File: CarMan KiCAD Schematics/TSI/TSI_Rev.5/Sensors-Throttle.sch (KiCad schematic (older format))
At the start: 56 parts, among them IC1 TS431ILT, J13 Conn_01x01, J24 Conn_01x01, J25 Conn_01x01, J26 J26, J27 J27, J28 Conn_01x01, U21 MCP6004, U25 NCD9830DBR2G, U26 MCP6004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

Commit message: - Updating TSI
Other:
- note added: "THROTTLE VOLTAGE ISOLATOR"
- note removed: "V/I\n& THROTTLE VOLTAGE ISOLATOR"
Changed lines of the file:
@@
 Text Notes 6950 6600 0    98   ~ 0
 Binary Address:\n1001010
-Text Notes 12100 10450 0    157  ~ 0
-V/I\n& THROTTLE VOLTAGE ISOLATOR
+Text Notes 12200 10350 0    157  ~ 0
+THROTTLE VOLTAGE ISOLATOR
 Text Label 6400 9600 2    50   ~ 0
 A2_HV

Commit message: Renumbered headers & changed some footprints
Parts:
- J24: renamed from J13; value Conn_01x01 -> MC+ Short Pin 1; footprint Connector_PinHeader_1.00mm:PinHeader_1x01_P1.00mm_Vertical -> Connector_PinSocket_2.54mm:PinSocket_1x01_P2.54mm_Vertical
- J25: renamed from J28; value Conn_01x01 -> MC+ Short Pin 2; footprint Connector_PinHeader_1.00mm:PinHeader_1x01_P1.00mm_Vertical -> Connector_PinSocket_2.54mm:PinSocket_1x01_P2.54mm_Vertical
- J26: value J26 -> HV+ Short Pin 1; footprint Connector_PinHeader_1.00mm:PinHeader_1x01_P1.00mm_Vertical -> Connector_PinSocket_2.54mm:PinSocket_1x01_P2.54mm_Vertical
- J27: renamed from J24; value Conn_01x01 -> HV+ Short Pin 2; footprint Connector_PinHeader_1.00mm:PinHeader_1x01_P1.00mm_Vertical -> Connector_PinSocket_2.54mm:PinSocket_1x01_P2.54mm_Vertical
- J28: renamed from J27; value J27 -> HV- Short Pin 1; footprint Connector_PinHeader_1.00mm:PinHeader_1x01_P1.00mm_Vertical -> Connector_PinSocket_2.54mm:PinSocket_1x01_P2.54mm_Vertical
- J29: renamed from J25; value Conn_01x01 -> HV- Short Pin 2; footprint Connector_PinHeader_1.00mm:PinHeader_1x01_P1.00mm_Vertical -> Connector_PinSocket_2.54mm:PinSocket_1x01_P2.54mm_Vertical
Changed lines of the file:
@@
 $Descr A3 16535 11693
 encoding utf-8
-Sheet 6 6
+Sheet 5 6
 Title ""
 Date ""
@@
 HV-
 $Comp
-L Connector_Generic:Conn_01x01 J24
+L Connector_Generic:Conn_01x01 J27
 U 1 1 5FA0FD5E
 P 14250 5700
-F 0 "J24" V 14350 5650 50  0000 L CNN
-F 1 "Conn_01x01" V 14350 5500 50  0001 L CNN
-F 2 "Connector_PinHeader_1.00mm:PinHeader_1x01_P1.00mm_Vertical" H 14250 5700 50  0001 C CNN
+F 0 "J27" V 14350 5650 50  0000 L CNN
+F 1 "HV+ Short Pin 2" V 14350 5500 50  0001 L CNN
+F 2 "Connector_PinSocket_2.54mm:PinSocket_1x01_P2.54mm_Vertical" H 14250 5700 50  0001 C CNN
 F 3 "~" H 14250 5700 50  0001 C CNN
 	1    14250 5700
@@
 	14250 5500 14200 5500
 $Comp
-L Connector_Generic:Conn_01x01 J28
+L Connector_Generic:Conn_01x01 J25
 U 1 1 5FA1321C
 P 14250 4800
-F 0 "J28" V 14350 4750 50  0000 L CNN
-F 1 "Conn_01x01" V 14213 4880 50  0001 L CNN
-F 2 "Connector_PinHeader_1.00mm:PinHeader_1x01_P1.00mm_Vertical" H 14250 4800 50  0001 C CNN
+F 0 "J25" V 14350 4750 50  0000 L CNN
+F 1 "MC+ Short Pin 2" V 14213 4880 50  0001 L CNN
+F 2 "Connector_PinSocket_2.54mm:PinSocket_1x01_P2.54mm_Vertical" H 14250 4800 50  0001 C CNN
 F 3 "~" H 14250 4800 50  0001 C CNN
 	1    14250 4800
@@
 	14250 6300 14200 6300
 $Comp
-L Connector_Generic:Conn_01x01 J25
+L Connector_Generic:Conn_01x01 J29
 U 1 1 5FA159E3
 P 14250 6500
-F 0 "J25" V 14350 6450 50  0000 L CNN
-F 1 "Conn_01x01" V 14350 6300 50  0001 L CNN
-F 2 "Connector_PinHeader_1.00mm:PinHeader_1x01_P1.00mm_Vertical" H 14250 6500 50  0001 C CNN
+F 0 "J29" V 14350 6450 50  0000 L CNN
+F 1 "HV- Short Pin 2" V 14350 6300 50  0001 L CNN
+F 2 "Connector_PinSocket_2.54mm:PinSocket_1x01_P2.54mm_Vertical" H 14250 6500 50  0001 C CNN
 F 3 "~" H 14250 6500 50  0001 C CNN
 	1    14250 6500
@@
 $EndComp
 $Comp
-L Connector_Generic:Conn_01x01 J27
+L Connector_Generic:Conn_01x01 J28
 U 1 1 5FA19A24
 P 12800 6500
-F 0 "J27" V 12900 6450 50  0000 L CNN
-F 1 "J27" V 12900 6300 50  0001 L CNN
-F 2 "Connector_PinHeader_1.00mm:PinHeader_1x01_P1.00mm_Vertical" H 12800 6500 50  0001 C CNN
+F 0 "J28" V 12900 6450 50  0000 L CNN
+F 1 "HV- Short Pin 1" V 12900 6300 50  0001 L CNN
+F 2 "Connector_PinSocket_2.54mm:PinSocket_1x01_P2.54mm_Vertical" H 12800 6500 50  0001 C CNN
 F 3 "~" H 12800 6500 50  0001 C CNN
 	1    12800 6500
@@
 P 12800 5700
 F 0 "J26" V 12900 5650 50  0000 L CNN
-F 1 "J26" V 12900 5500 50  0001 L CNN
-F 2 "Connector_PinHeader_1.00mm:PinHeader_1x01_P1.00mm_Vertical" H 12800 5700 50  0001 C CNN
+F 1 "HV+ Short Pin 1" V 12900 5500 50  0001 L CNN
+F 2 "Connector_PinSocket_2.54mm:PinSocket_1x01_P2.54mm_Vertical" H 12800 5700 50  0001 C CNN
 F 3 "~" H 12800 5700 50  0001 C CNN
 	1    12800 5700
@@
 	12800 5500 12850 5500
 $Comp
-L Connector_Generic:Conn_01x01 J13
+L Connector_Generic:Conn_01x01 J24
 U 1 1 5FA20DB0
 P 12800 4800
-F 0 "J13" V 12900 4750 50  0000 L CNN
-F 1 "Conn_01x01" V 12900 4600 50  0001 L CNN
-F 2 "Connector_PinHeader_1.00mm:PinHeader_1x01_P1.00mm_Vertical" H 12800 4800 50  0001 C CNN
+F 0 "J24" V 12900 4750 50  0000 L CNN
+F 1 "MC+ Short Pin 1" V 12900 4600 50  0001 L CNN
+F 2 "Connector_PinSocket_2.54mm:PinSocket_1x01_P2.54mm_Vertical" H 12800 4800 50  0001 C CNN
 F 3 "~" H 12800 4800 50  0001 C CNN
 	1    12800 4800

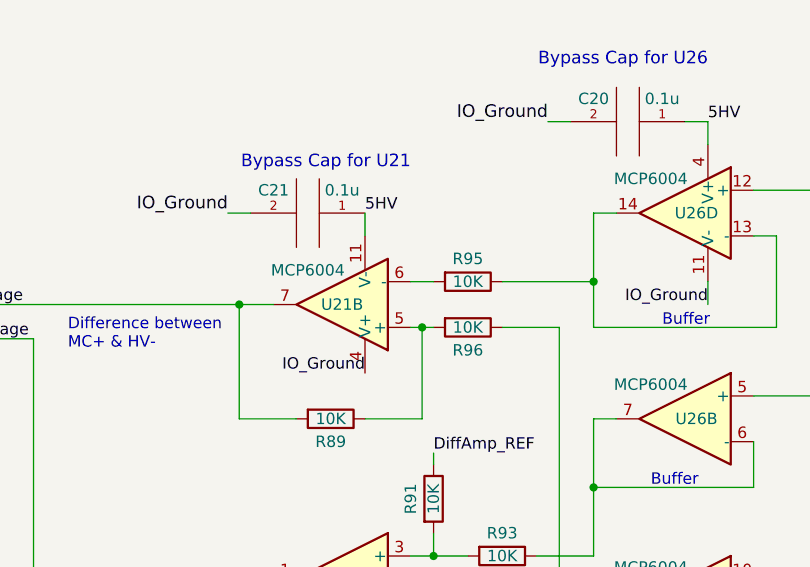
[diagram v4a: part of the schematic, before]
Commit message: - Added pull up resistor to U21B differential circuit - Removed zener across PC relay
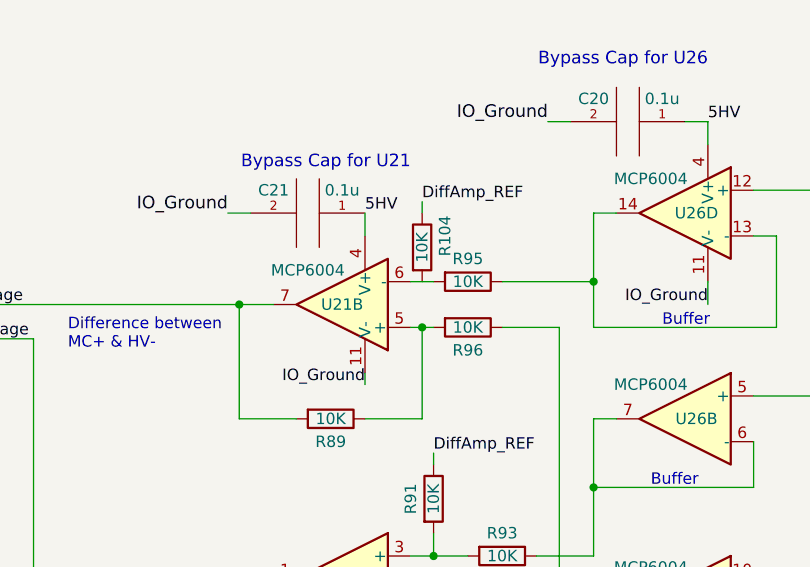
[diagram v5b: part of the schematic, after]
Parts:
- added R104: 10K, Resistor_SMD:R_0805_2012Metric_Pad1.15x1.40mm_HandSolder, symbol Device:R
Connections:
- wire segments 195 -> 197
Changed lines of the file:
@@
 Wire Wire Line
 	10100 4800 10100 4700
-Text Label 10100 5400 2    50   ~ 0
+Text Label 10100 5450 2    50   ~ 0
 IO_Ground
 $Comp
@@
 L Amplifier_Operational:MCP6004 U21
 U 5 1 5F997C97
-P 10000 5100
-F 0 "U21" H 9958 5146 50  0001 L CNN
-F 1 "MCP6004" H 9958 5100 50  0001 L CNN
-F 2 "TSI_Rev_2021_Footprint_Lib:SOIC127P600X175-14N" H 9950 5200 50  0001 C CNN
-F 3 "http://ww1.microchip.com/downloads/en/DeviceDoc/21733j.pdf" H 10050 5300 50  0001 C CNN
-	5    10000 5100
-	-1   0    0    1
+P 10200 5100
+F 0 "U21" H 10158 5146 50  0001 L CNN
+F 1 "MCP6004" H 10158 5100 50  0001 L CNN
+F 2 "TSI_Rev_2021_Footprint_Lib:SOIC127P600X175-14N" H 10150 5200 50  0001 C CNN
+F 3 "http://ww1.microchip.com/downloads/en/DeviceDoc/21733j.pdf" H 10250 5300 50  0001 C CNN
+	5    10200 5100
+	1    0    0    -1
 $EndComp
 $Comp
@@
 Wire Notes Line
 	1400 8350 1400 9250
+Wire Wire Line
+	10100 5450 10100 5400
+Text Label 10350 4650 0    50   ~ 0
+DiffAmp_REF
+Wire Wire Line
+	10350 4650 10350 4700
+$Comp
+L Device:R R104
+U 1 1 60749BC2
+P 10350 4850
+F 0 "R104" V 10450 4900 50  0000 C CNN
+F 1 "10K" V 10350 4850 50  0000 C CNN
+F 2 "Resistor_SMD:R_0805_2012Metric_Pad1.15x1.40mm_HandSolder" V 10280 4850 50  0001 C CNN
+F 3 "~" H 10350 4850 50  0001 C CNN
+	1    10350 4850
+	1    0    0    -1
+$EndComp
 $EndSCHEMATC

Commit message: - Removing IC1/ Diffamp_Ref (1.24V)
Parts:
- removed IC1: TS431ILT, TSI_Rev_2021_Footprint_Lib:SOT95P280X145-5N, symbol CarMan_KiCAD_Library:TS431ILT
- removed R103: 1K, Resistor_SMD:R_0805_2012Metric_Pad1.15x1.40mm_HandSolder, symbol Device:R
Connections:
- net labels added: 1.24HV_REF
- net labels removed: 1.24V_REF
- wire segments 197 -> 189
- no-connect marks 6 -> 4
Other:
- note removed: "(1.24V)\n"
- note removed: "1.24V Voltage Reference\n"
- note removed: "VOLTAGE REFERENCE"
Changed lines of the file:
@@
 Text Label 6750 6000 2    50   ~ 0
 5HV
-Text Label 14800 8800 0    50   ~ 0
-IO_Ground
-NoConn ~ 14050 8800
-NoConn ~ 14050 8900
-Wire Wire Line
-	13900 8550 13900 9000
-Wire Wire Line
-	14800 8800 14750 8800
-Wire Wire Line
-	13900 8200 13900 8550
-Connection ~ 13900 8550
-Text Label 13900 8300 0    50   ~ 0
-DiffAmp_REF
-Text Notes 14000 8400 0    50   ~ 0
-(1.24V)\n
-$Comp
-L Device:R R103
-U 1 1 5FBCE887
-P 13650 9000
-F 0 "R103" V 13550 9000 50  0000 C CNN
-F 1 "1K" V 13650 9000 50  0000 C CNN
-F 2 "Resistor_SMD:R_0805_2012Metric_Pad1.15x1.40mm_HandSolder" V 13580 9000 50  0001 C CNN
-F 3 "~" H 13650 9000 50  0001 C CNN
-	1    13650 9000
-	0    1    1    0
-$EndComp
-Wire Wire Line
-	13350 9000 13500 9000
-Wire Wire Line
-	13800 9000 13900 9000
-Connection ~ 13900 9000
-Wire Wire Line
-	13900 9000 14050 9000
-Text Label 13350 9000 2    50   ~ 0
-5HV
-Text Notes 14900 9400 2    50   ~ 0
-1.24V Voltage Reference\n
 Wire Notes Line
 	4000 450  4000 11100
@@
 Text HLabel 2100 9150 0    50   Input ~ 0
 Throttle_LV
-Text HLabel 5750 9700 0    50   Output ~ 0
-1.24V_REF
+Text HLabel 5750 9700 0    50   Input ~ 0
+1.24HV_REF
 Text HLabel 5750 8800 0    50   Input ~ 0
 IO_Ground
@@
 Throttle_HV
 Text Label 6400 9700 2    50   ~ 0
-DiffAmp_REF
+1.24HV_REF
 Text Label 6400 8700 2    50   ~ 0
 5HV
@@
 Text HLabel 5750 9300 0    50   Input ~ 0
 HV-
-Wire Notes Line
-	12650 9650 15850 9650
-Wire Notes Line
-	15850 9650 15850 7450
-Wire Notes Line
-	15850 7450 12650 7450
-Wire Notes Line
-	12650 7450 12650 9650
-Text Notes 13450 7650 0    98   ~ 0
-VOLTAGE REFERENCE
 Wire Wire Line
 	2500 5400 3500 5400
@@
 Wire Wire Line
 	11600 5100 11600 5000
-$Comp
-L power:PWR_FLAG #FLG0104
-U 1 1 6112F663
-P 13900 8200
-F 0 "#FLG0104" H 13900 8275 50  0001 C CNN
-F 1 "PWR_FLAG" H 13900 8373 50  0000 C CNN
-F 2 "" H 13900 8200 50  0001 C CNN
-F 3 "~" H 13900 8200 50  0001 C CNN
-	1    13900 8200
-	1    0    0    -1
-$EndComp
 Text Notes 3550 5100 0    47   ~ 0
 I2C Isolator\n
-$Comp
-L CarMan_KiCAD_Library:TS431ILT IC1
-U 1 1 61439D09
-P 14400 8900
-F 0 "IC1" H 14400 9150 79  0000 C CNN
-F 1 "TS431ILT" H 14400 8600 79  0000 C CNN
-F 2 "TSI_Rev_2021_Footprint_Lib:SOT95P280X145-5N" H 14150 9000 79  0001 C CNN
-F 3 "https://www.snapeda.com/parts/TS431ILT/STMicroelectronics/datasheet/" H 14150 9000 79  0001 C CNN
-	1    14400 8900
-	1    0    0    -1
-$EndComp
-Wire Wire Line
-	14750 9000 15300 9000
-Wire Wire Line
-	13900 8550 15300 8550
-Wire Wire Line
-	15300 8550 15300 9000
 Text Label 4800 1350 0    50   ~ 0
 5HV
@@
 	1    0    0    -1
 $EndComp
+Text Label 11125 3450 0    50   ~ 0
+DiffAmp_REF
+Text Label 12225 3450 2    50   ~ 0
+1.24HV_REF
+Wire Wire Line
+	11125 3450 12225 3450
 $EndSCHEMATC

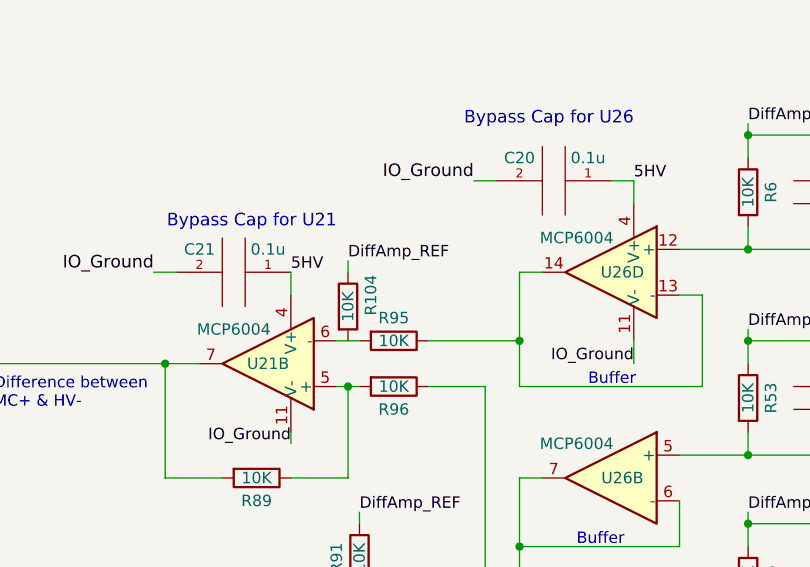
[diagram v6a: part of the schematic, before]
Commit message: - Added a Throttle Plausible Green LED
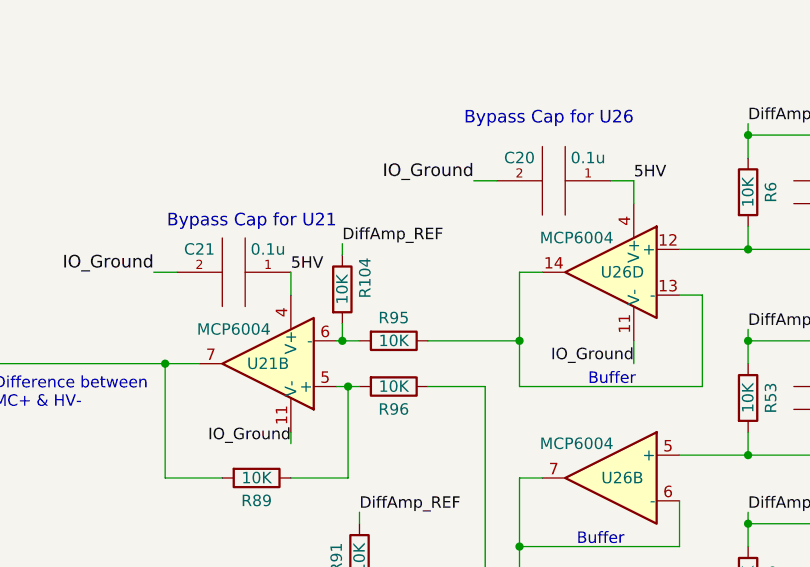
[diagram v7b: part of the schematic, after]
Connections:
- net at R95.2, U21.6 (-): now also R104.2
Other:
- moved on the sheet: R104
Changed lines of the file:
@@
 $EndComp
-Wire Wire Line
-	10400 5000 10300 5000
 Wire Wire Line
 	11100 5000 11100 4700
@@
 Wire Wire Line
 	10100 5450 10100 5400
-Text Label 10350 4650 0    50   ~ 0
+Text Label 10325 4575 0    50   ~ 0
 DiffAmp_REF
 Wire Wire Line
-	10350 4650 10350 4700
+	10325 4575 10325 4625
 $Comp
 L Device:R R104
 U 1 1 60749BC2
-P 10350 4850
-F 0 "R104" V 10450 4900 50  0000 C CNN
-F 1 "10K" V 10350 4850 50  0000 C CNN
-F 2 "Resistor_SMD:R_0805_2012Metric_Pad1.15x1.40mm_HandSolder" V 10280 4850 50  0001 C CNN
-F 3 "~" H 10350 4850 50  0001 C CNN
-	1    10350 4850
+P 10325 4775
+F 0 "R104" V 10425 4825 50  0000 C CNN
+F 1 "10K" V 10325 4775 50  0000 C CNN
+F 2 "Resistor_SMD:R_0805_2012Metric_Pad1.15x1.40mm_HandSolder" V 10255 4775 50  0001 C CNN
+F 3 "~" H 10325 4775 50  0001 C CNN
+	1    10325 4775
 	1    0    0    -1
 $EndComp
@@
 Wire Wire Line
 	11125 3450 12225 3450
+Wire Wire Line
+	10300 5000 10325 5000
+Wire Wire Line
+	10325 5000 10325 4925
+Connection ~ 10325 5000
+Wire Wire Line
+	10325 5000 10400 5000
 $EndSCHEMATC

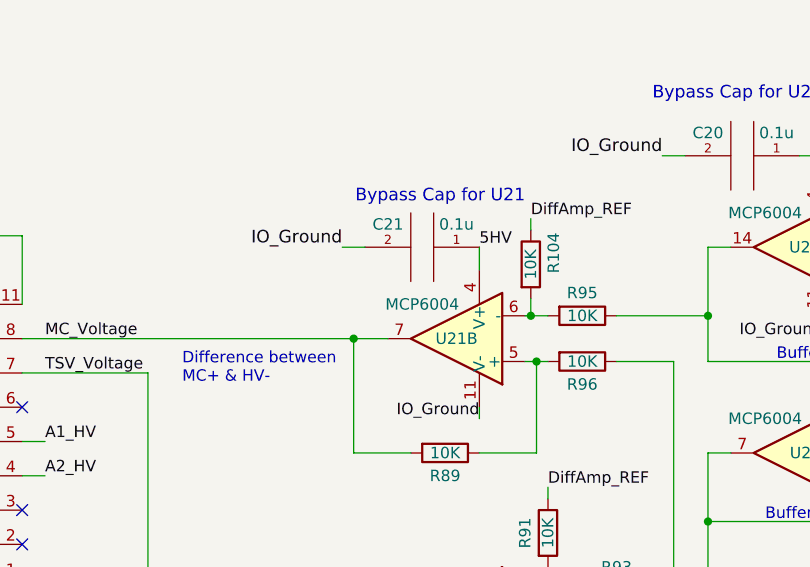
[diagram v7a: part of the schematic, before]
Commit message: Fixed Throttle Voltage Iso, U21B had the wrong inputs to the +/- terminals
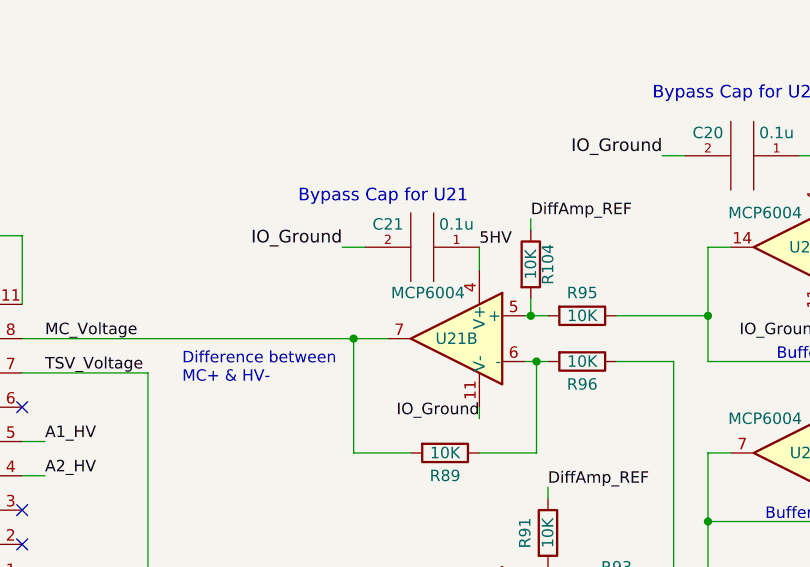
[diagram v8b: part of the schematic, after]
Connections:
- net at R89.1, R96.2: now also U21.6 (-); no longer U21.5 (+)
- net at R104.2, R95.2: now also U21.5 (+); no longer U21.6 (-)
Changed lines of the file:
@@
 Wire Wire Line
 	9500 4700 9600 4700
-Text Notes 10300 4600 2    55   ~ 0
+Text Notes 10050 4600 2    55   ~ 0
 Bypass Cap for U21\n\n
 $Comp
@@
 P 10000 5100
 F 0 "U21" H 10000 5100 50  0000 C CNN
-F 1 "MCP6004" H 10150 4950 50  0000 C CNN
+F 1 "MCP6004" H 10125 5300 50  0000 C CNN
 F 2 "TSI_Rev_2021_Footprint_Lib:SOIC127P600X175-14N" H 9950 5200 50  0001 C CNN
 F 3 "http://ww1.microchip.com/downloads/en/DeviceDoc/21733j.pdf" H 10050 5300 50  0001 C CNN
 	2    10000 5100
-	-1   0    0    1
+	-1   0    0    -1
 $EndComp
 Text Label 10100 4700 0    50   ~ 0
@@
 U 1 1 60749BC2
 P 10325 4775
-F 0 "R104" V 10425 4825 50  0000 C CNN
+F 0 "R104" V 10400 4775 50  0000 C CNN
 F 1 "10K" V 10325 4775 50  0000 C CNN
 F 2 "Resistor_SMD:R_0805_2012Metric_Pad1.15x1.40mm_HandSolder" V 10255 4775 50  0001 C CNN
